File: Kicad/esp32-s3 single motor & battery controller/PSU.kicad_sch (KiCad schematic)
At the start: 73 parts, among them J5 Batt Balance connector, Q1 NMOS,12v, Q2 NMOS, 12v, Q3 NMOS,12v,PPak, Q4 NMOS, 12v, Q5 NMOS, 12v, Q7 NMOS,12v,PPak, U2 AP63203WU, U3 BQ76905RGRR, U4 BQ24780SRUYR

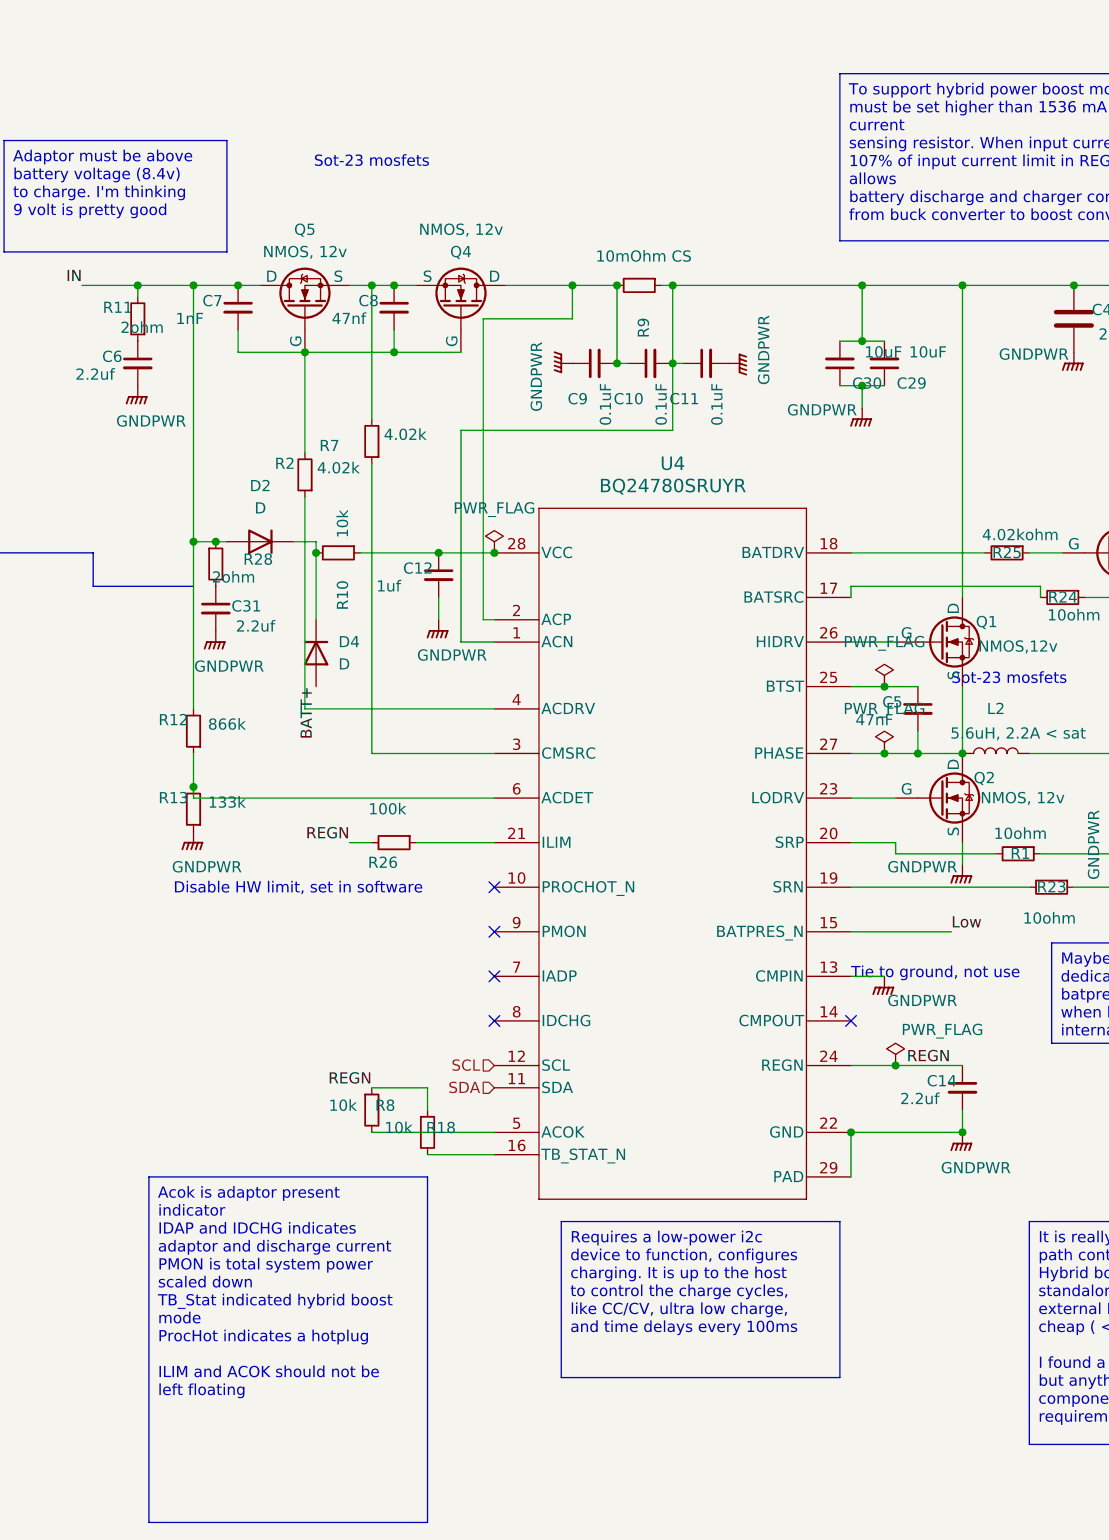
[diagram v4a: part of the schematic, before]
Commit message: Making a few changes to layout based on spotted problems
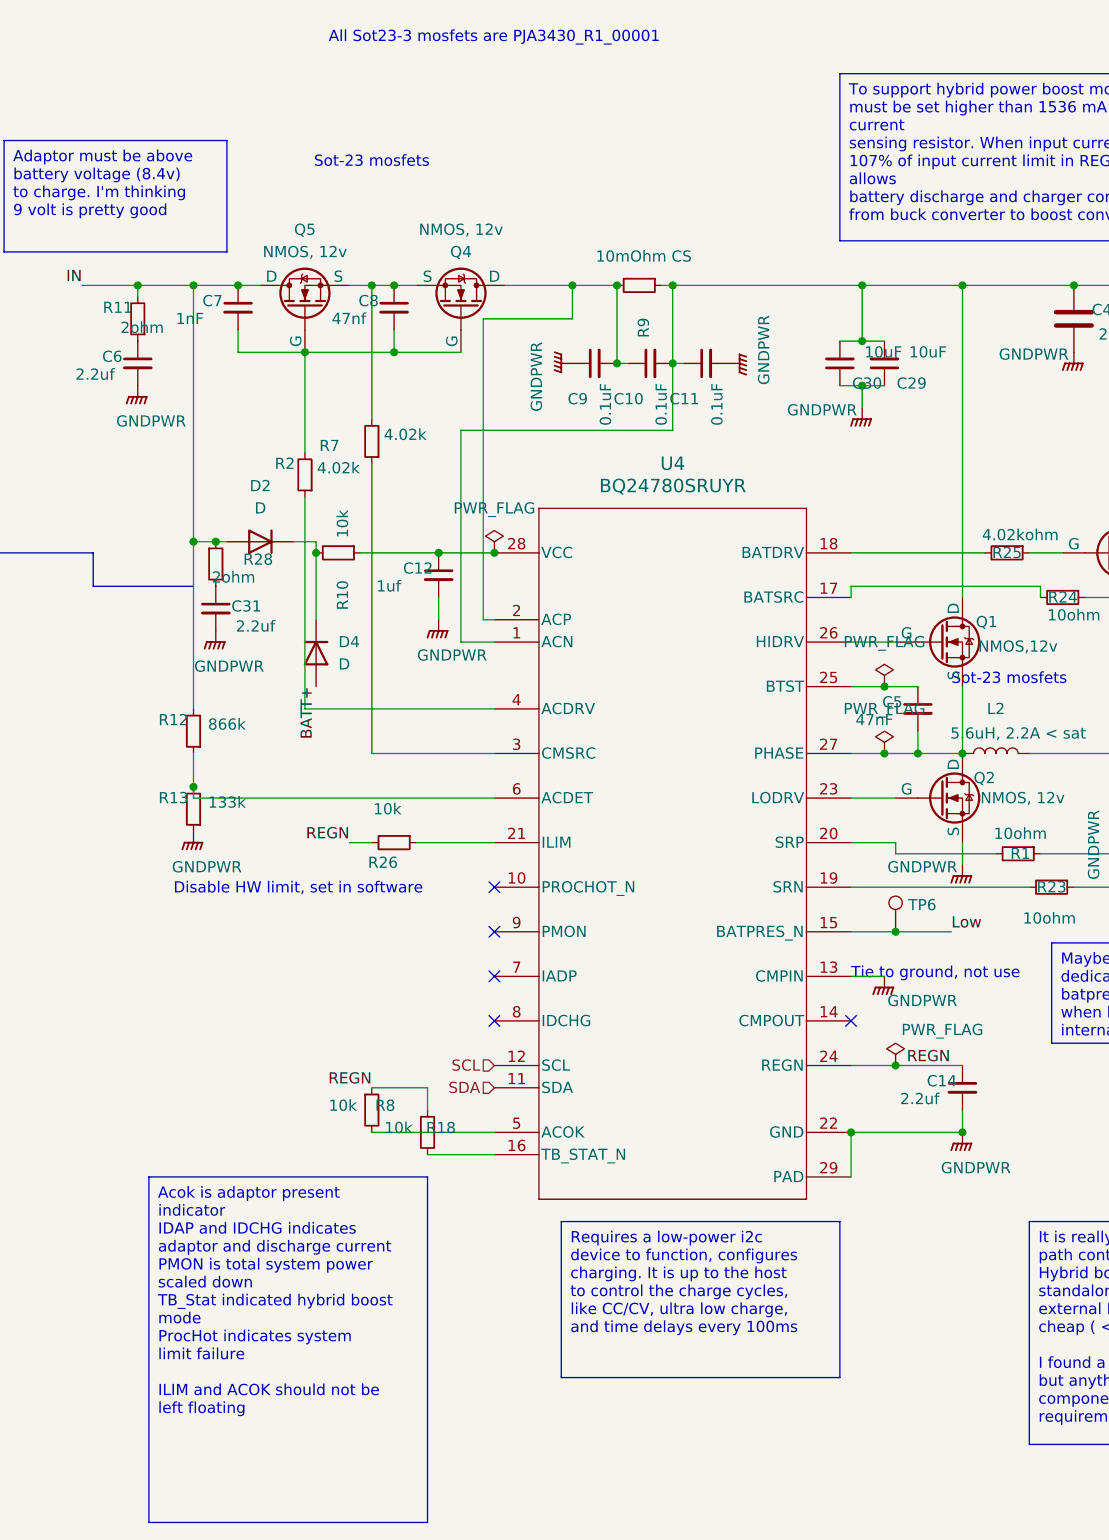
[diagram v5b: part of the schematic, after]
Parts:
- added TP6: ~, TestPoint:TestPoint_Pad_D1.0mm, symbol Connector:TestPoint
- R26: value 100k -> 10k
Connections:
- net Low: now also TP6.1
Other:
- note added: "All Sot23-3 mosfets are PJA3430_R1_00001"
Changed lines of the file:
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@@
 	)
 	(junction
+		(at 99.06 138.43)
+		(diameter 0)
+		(color 0 0 0 0)
+	)
+	(junction
 		(at 93.98 161.29)
 		(diameter 0)
@@
 	(wire
 		(pts
-			(xy 93.98 138.43) (xy 105.41 138.43)
+			(xy 93.98 138.43) (xy 99.06 138.43)
 		)
 		(stroke
@@
 	(wire
 		(pts
+			(xy 99.06 138.43) (xy 105.41 138.43)
+		)
+		(stroke
+			(width 0)
+			(type default)
+		)
+	)
+	(wire
+		(pts
 			(xy 137.16 118.11) (xy 144.78 118.11)
 		)
@@
 		)
 	)
-	(text_box "Acok is adaptor present indicator\nIDAP and IDCHG indicates adaptor and discharge current\nPMON is total system power scaled down\nTB_Stat indicated hybrid boost mode\nProcHot indicates a hotplug\n\nILIM and ACOK should not be left floating "
+	(text_box "Acok is adaptor present indicator\nIDAP and IDCHG indicates adaptor and discharge current\nPMON is total system power scaled down\nTB_Stat indicated hybrid boost mode\nProcHot indicates system limit failure\n\nILIM and ACOK should not be left floating "
 		(exclude_from_sim no)
 		(at 13.97 166.37 0)
@@
 		)
 	)
+	(text "All Sot23-3 mosfets are PJA3430_R1_00001"
+		(exclude_from_sim no)
+		(at 53.34 36.576 0)
+		(effects
+			(font
+				(size 1.27 1.27)
+			)
+		)
+	)
 	(text "Tie to ground, not use"
 		(exclude_from_sim no)
@@
 	)
 	(symbol
+		(lib_id "Connector:TestPoint")
+		(at 99.06 138.43 0)
+		(unit 1)
+		(exclude_from_sim no)
+		(in_bom yes)
+		(on_board yes)
+		(dnp no)
+		(property "Reference" "TP6"
+			(at 102.108 135.382 0)
+			(effects
+				(font
+					(size 1.27 1.27)
+				)
+			)
+		)
+		(property "Value" "~"
+			(at 99.314 129.54 90)
+			(effects
+				(font
+					(size 1.27 1.27)
+				)
+			)
+		)
+		(property "Footprint" "TestPoint:TestPoint_Pad_D1.0mm"
+			(at 104.14 138.43 0)
+			(effects
+				(font
+					(size 1.27 1.27)
+				)
+				(hide yes)
+			)
+		)
+		(property "Datasheet" "~"
+			(at 104.14 138.43 0)
+			(effects
+				(font
+					(size 1.27 1.27)
+				)
+				(hide yes)
+			)
+		)
+		(property "Description" "test point"
+			(at 99.06 138.43 0)
+			(effects
+				(font
+					(size 1.27 1.27)
+				)
+				(hide yes)
+			)
+		)
+		(pin "1"
+		)
+		(instances
+			(project "esp32-s3 single motor & battery controller"
+				(path "/eb3f183d-8bb1-43a5-a363-092ed67891e3/a57a0b4f-e246-497c-8d94-688647d8fd03"
+					(reference "TP6")
+					(unit 1)
+				)
+			)
+		)
+	)
+	(symbol
 		(lib_id "Simulation_SPICE:NMOS")
 		(at 31.75 67.31 90)
@@
 			)
 		)
-		(property "Value" "100k"
+		(property "Value" "10k"
 			(at 41.148 124.46 90)
 			(effects

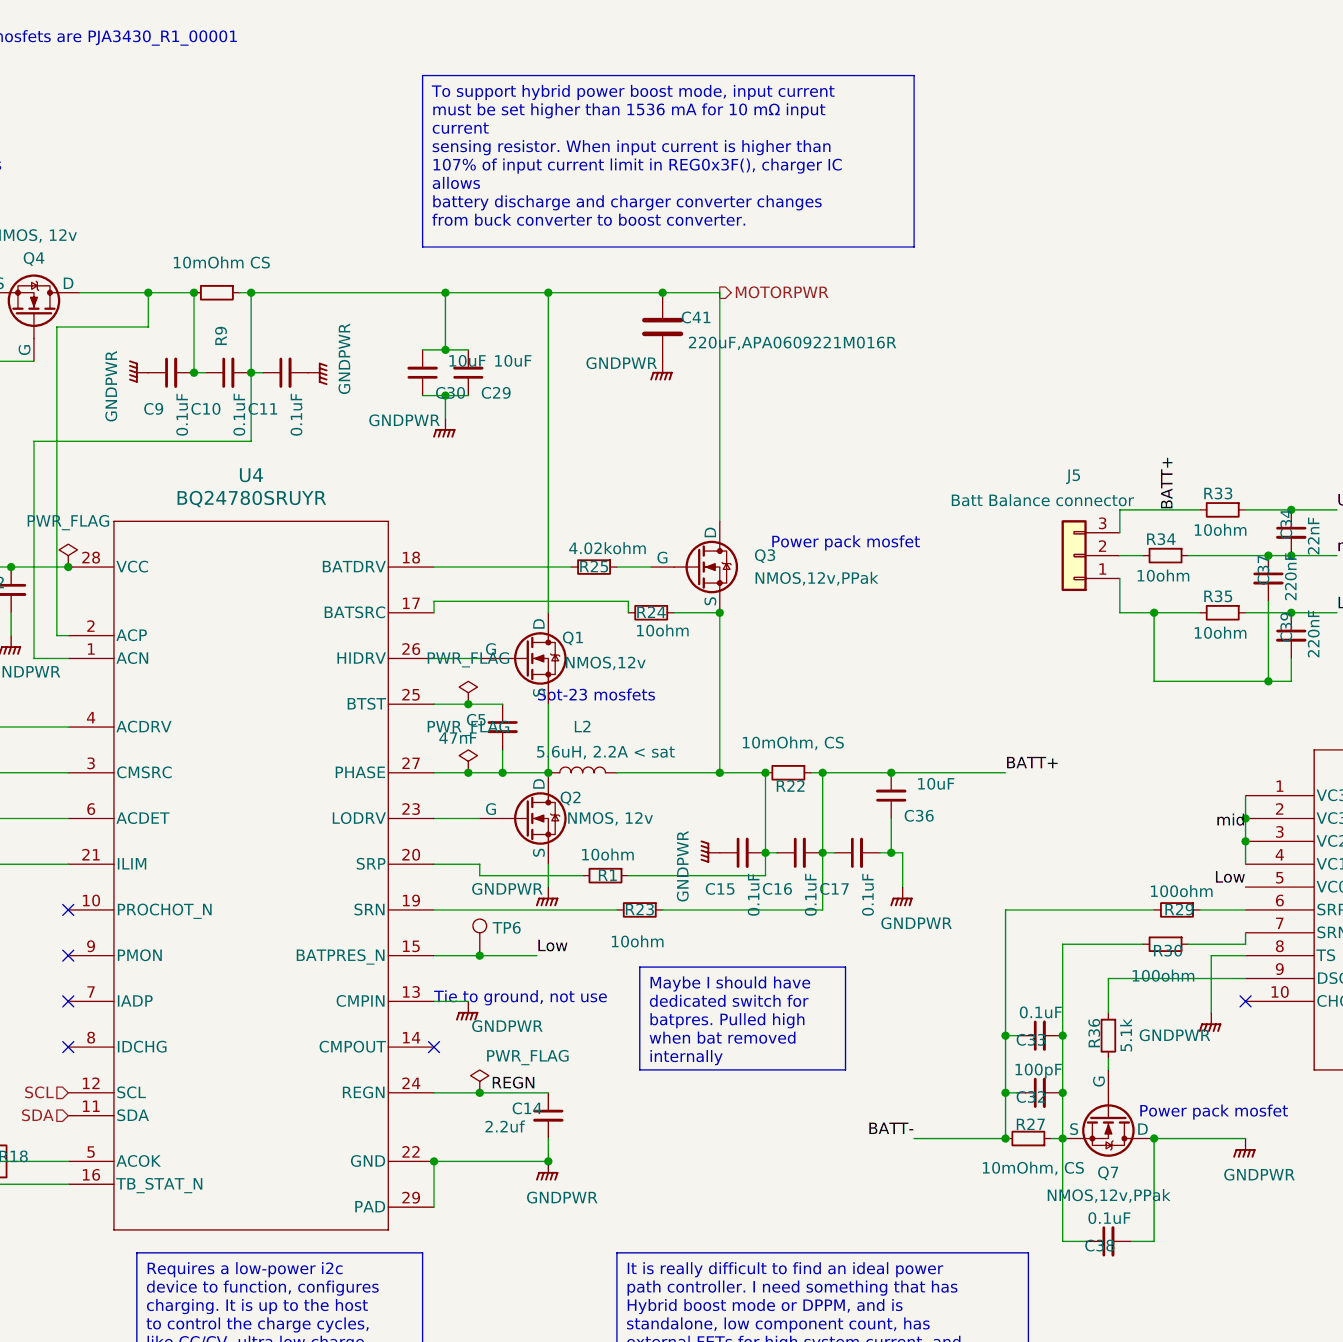
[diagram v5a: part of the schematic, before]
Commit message: Replacing sense resistors, started routing additional pullup resistors
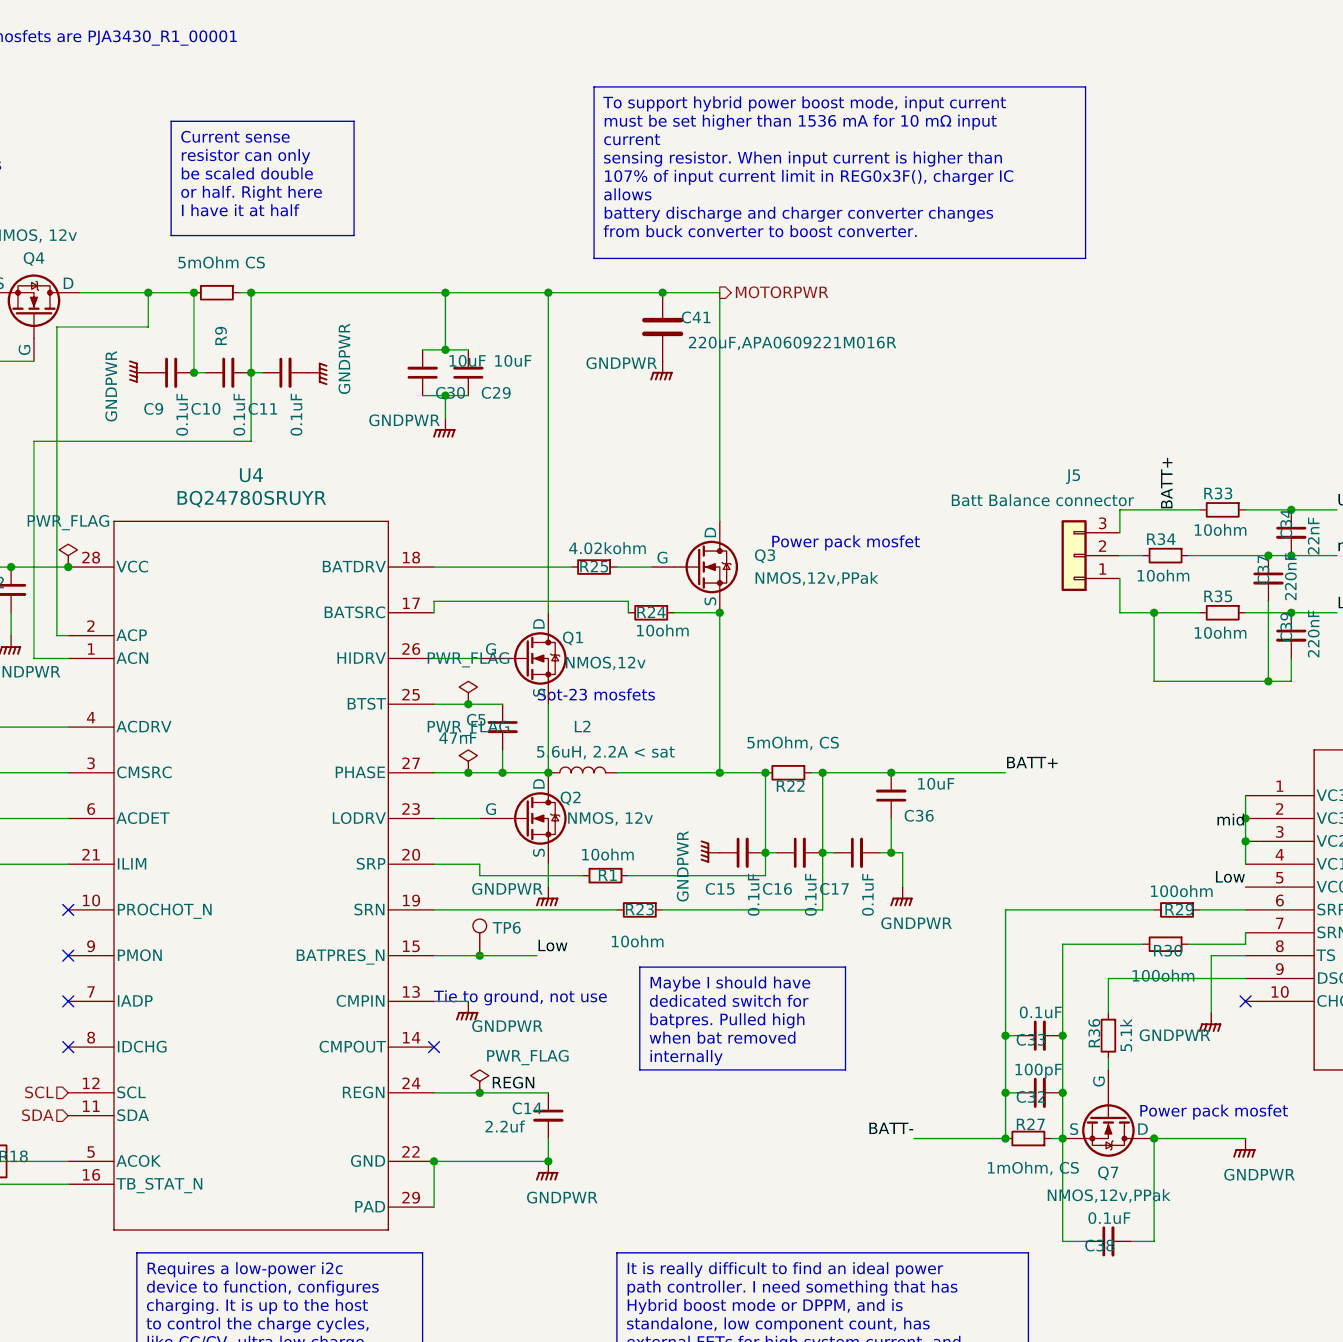
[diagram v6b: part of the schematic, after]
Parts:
- R22: value 10mOhm, CS -> 5mOhm, CS
- R27: value 10mOhm, CS -> 1mOhm, CS
- R9: value 10mOhm CS -> 5mOhm CS
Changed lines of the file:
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@@
+		)
+	)
+	(text_box "Current sense resistor can only be scaled double or half. Right here I have it at half"
+		(exclude_from_sim no)
+		(at 64.77 45.72 0)
+		(size 20.32 12.7)
+		(stroke
+			(width 0)
+			(type default)
+		)
+		(fill
+			(type none)
+		)
+		(effects
+			(font
+				(size 1.27 1.27)
+			)
+			(justify left top)
 		)
 	)
 	(text_box "To support hybrid power boost mode, input current must be set higher than 1536 mA for 10 mΩ input current\nsensing resistor. When input current is higher than 107% of input current limit in REG0x3F(), charger IC allows\nbattery discharge and charger converter changes from buck converter to boost converter."
 		(exclude_from_sim no)
-		(at 92.71 40.64 0)
+		(at 111.76 41.91 0)
 		(size 54.61 19.05)
 		(stroke
@@
 			)
 		)
-		(property "Value" "10mOhm, CS"
+		(property "Value" "1mOhm, CS"
 			(at 160.528 162.052 90)
 			(effects
@@
 			)
 		)
-		(property "Value" "10mOhm CS"
+		(property "Value" "5mOhm CS"
 			(at 70.358 61.468 90)
 			(effects
@@
 			)
 		)
-		(property "Value" "10mOhm, CS"
+		(property "Value" "5mOhm, CS"
 			(at 133.858 114.808 90)
 			(effects

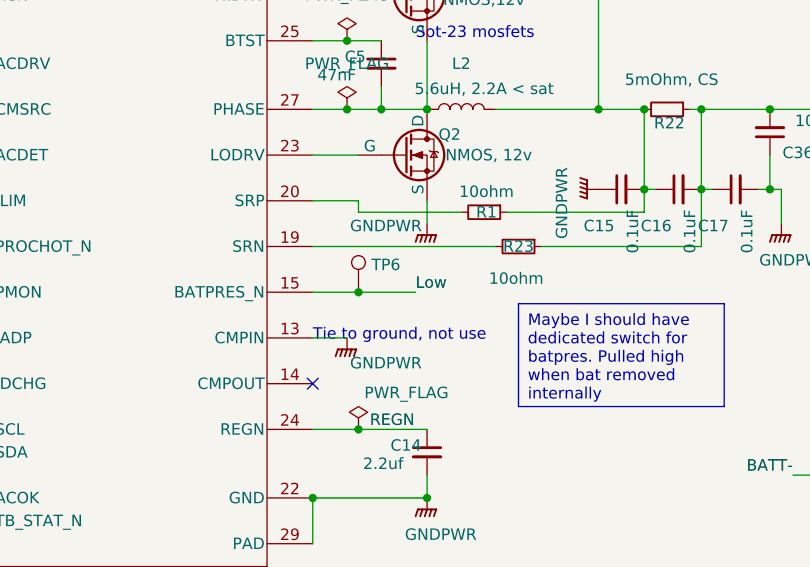
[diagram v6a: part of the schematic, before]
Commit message: Routed pullup resistors, replace Bat Pres trace with pad
I now have several lines routed on the ground plane, but I tried to minimize the used space
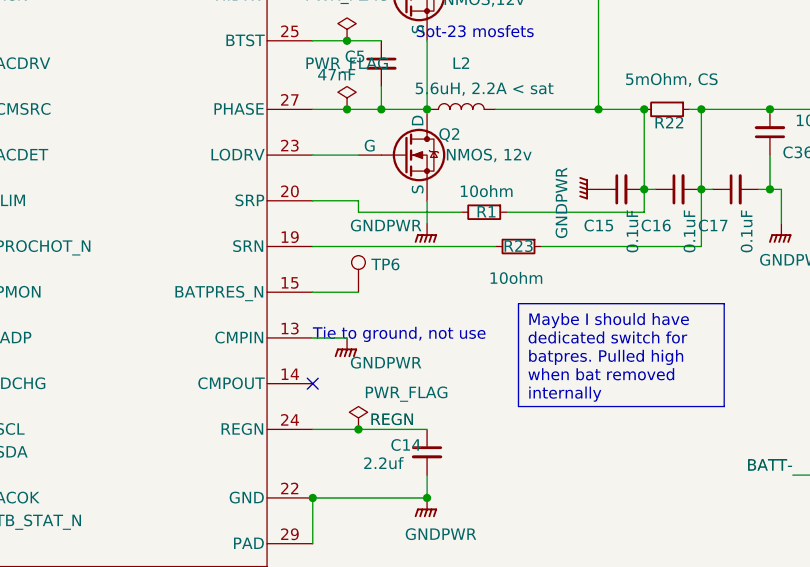
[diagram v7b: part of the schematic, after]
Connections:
- net Low: no longer TP6.1, U4.15 (BATPRES_N)
- new net: TP6.1, U4.15 (BATPRES_N)
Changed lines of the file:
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@@
-	)
-	(junction
-		(at 99.06 138.43)
-		(diameter 0)
-		(color 0 0 0 0)
 	)
 	(junction
@@
 		(pts
 			(xy 30.48 93.98) (xy 33.02 93.98)
-		)
-		(stroke
-			(width 0)
-			(type default)
-		)
-	)
-	(wire
-		(pts
-			(xy 99.06 138.43) (xy 105.41 138.43)
 		)
 		(stroke
@@
 		)
 	)
-	(label "Low"
-		(at 105.41 138.43 0)
-		(fields_autoplaced yes)
-		(effects
-			(font
-				(size 1.27 1.27)
-			)
-			(justify left bottom)
-		)
-	)
